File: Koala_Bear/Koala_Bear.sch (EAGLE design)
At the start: 15 parts

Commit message: Added Koala
Change-Id: I1ccdab2cf6fbd4164808b8b310fecc799373998b
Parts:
- removed JP1: (no value), pie:M03MTA1X3
- removed U$2: XT60CONNECTOR, pie:XT60CONNECTOR
- removed U$8: M05, pie:M05
- added MSTRO_PINS: (no value), pie_new:M041X04-MTA
- added MSTRO_PWR: M05, pie:M05
- added SERVO_PWR_12, SERVO_PWR_6: (no value), pie:M02PTH
- added XT60: XT60CONNECTOR, pie_new:XT60CONNECTOR
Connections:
- net N$1 renamed EN
- net N$3 renamed DIODE
- removed net N$5: JP1.3, U$8.1
- new net N$3: MSTRO_PINS.3, MSTRO_PWR.2
- net GND: now also MSTRO_PINS.1, MSTRO_PWR.5, SERVO_PWR_12.1, SERVO_PWR_6.2, XT60.GND; no longer U$2.GND, U$8.5
- net N$2: now also MSTRO_PINS.2, MSTRO_PWR.3; no longer JP1.1, U$8.3
- net N$4: now also MSTRO_PINS.4, MSTRO_PWR.1; no longer JP1.2, U$8.2
- net VIN: now also XT60.12V; no longer U$2.12V
- net VOUT: now also MSTRO_PWR.4, SERVO_PWR_12.2, SERVO_PWR_6.1; no longer U$8.4
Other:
- note added: "BATTERY"
- moved on the sheet: CFF, CIN, COUT1, COUT2, CSS, D1, REN1, REN2, REN3, RFBB, RFBT

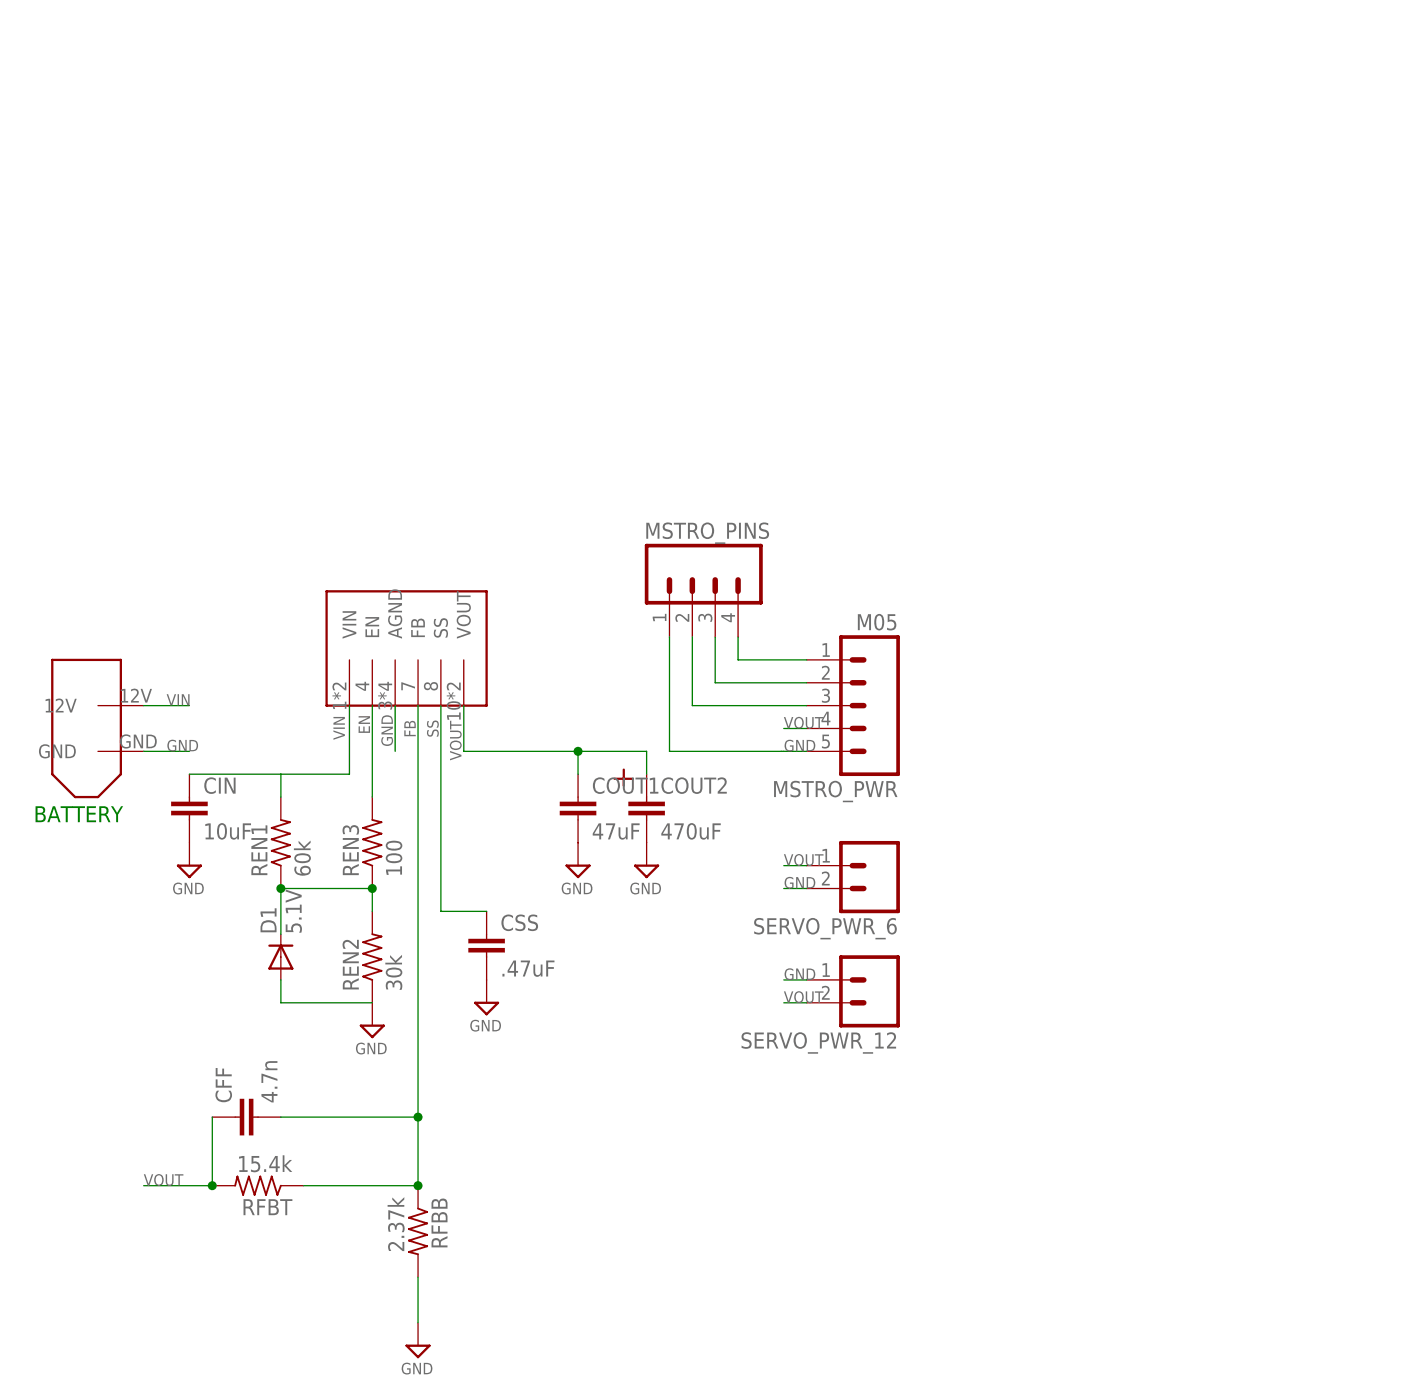
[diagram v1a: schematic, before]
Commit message: Added preliminary LED system. Incomplete.
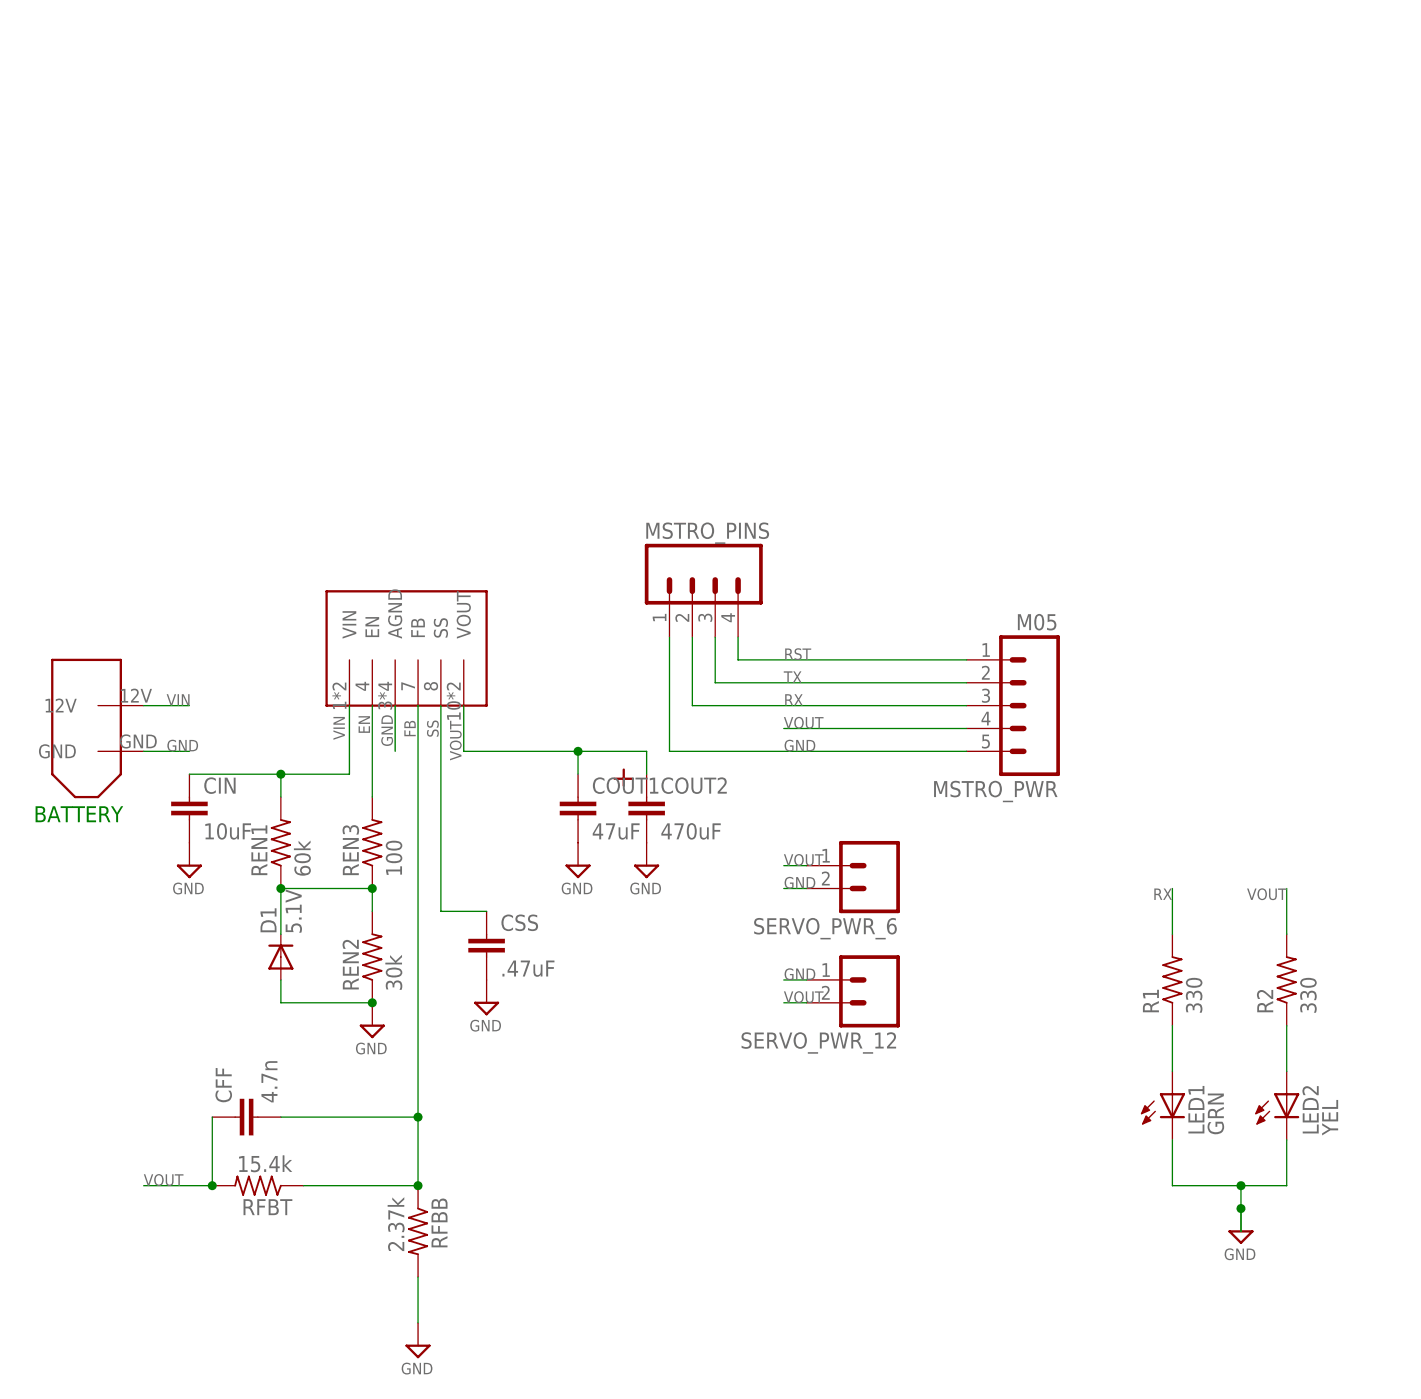
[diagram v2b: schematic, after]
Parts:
- added LED1: GRN, led:LEDCHIP-LED0805
- added LED2: YEL, led:LEDCHIP-LED0805
- added R1, R2: 330, rcl:R-US_R0603
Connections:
- net N$3 renamed TX
- net N$4 renamed RST
- removed net N$2: MSTRO_PINS.2, MSTRO_PWR.3
- new net N$1: LED1.A, R1.1
- new net N$5: LED2.A, R2.1
- new net RX: MSTRO_PINS.2, MSTRO_PWR.3, R1.2
- net GND: now also LED1.C, LED2.C
- net VOUT: now also R2.2
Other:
- moved on the sheet: MSTRO_PWR
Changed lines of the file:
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@@
 <?xml version="1.0" encoding="utf-8"?>
 <!DOCTYPE eagle SYSTEM "eagle.dtd">
-<eagle version="6.2">
+<eagle version="6.5.0">
 <drawing>
 <settings>
@@
 <part name="SERVO_PWR_12" library="pie" deviceset="M02" device="PTH"/>
 <part name="FRAME1" library="pie" deviceset="FRAME-LETTER" device=""/>
+<part name="R1" library="rcl" deviceset="R-US_" device="R0603" value="330"/>
+<part name="R2" library="rcl" deviceset="R-US_" device="R0603" value="330"/>
+<part name="LED1" library="led" deviceset="LED" device="CHIP-LED0805" value="GRN"/>
+<part name="LED2" library="led" deviceset="LED" device="CHIP-LED0805" value="YEL"/>
+<part name="SUPPLY4" library="supply2" deviceset="GND" device=""/>
 </parts>
 <sheets>
@@
 </instance>
 <instance part="XT60" gate="G$1" x="-25.4" y="50.8" smashed="yes" rot="R270"/>
-<instance part="MSTRO_PWR" gate="G$1" x="63.5" y="43.18" smashed="yes" rot="R180">
-<attribute name="VALUE" x="68.58" y="55.88" size="1.778" layer="96" font="vector" rot="R180"/>
-<attribute name="NAME" x="68.58" y="37.338" size="1.778" layer="95" font="vector" rot="R180"/>
+<instance part="MSTRO_PWR" gate="G$1" x="81.28" y="43.18" smashed="yes" rot="R180">
+<attribute name="VALUE" x="86.36" y="55.88" size="1.778" layer="96" font="vector" rot="R180"/>
+<attribute name="NAME" x="86.36" y="37.338" size="1.778" layer="95" font="vector" rot="R180"/>
 </instance>
 <instance part="SERVO_PWR_6" gate="G$1" x="66.04" y="27.94" smashed="yes" rot="R180">
@@
 <attribute name="DRAWING_NAME" x="73.914" y="-66.04" size="2.7432" layer="94" font="vector"/>
 </instance>
+<instance part="R1" gate="G$1" x="99.06" y="15.24" smashed="yes" rot="R90">
+<attribute name="NAME" x="97.5614" y="11.43" size="1.778" layer="95" rot="R90"/>
+<attribute name="VALUE" x="102.362" y="11.43" size="1.778" layer="96" rot="R90"/>
+</instance>
+<instance part="R2" gate="G$1" x="111.76" y="15.24" smashed="yes" rot="R90">
+<attribute name="NAME" x="110.2614" y="11.43" size="1.778" layer="95" rot="R90"/>
+<attribute name="VALUE" x="115.062" y="11.43" size="1.778" layer="96" rot="R90"/>
+</instance>
+<instance part="LED1" gate="G$1" x="99.06" y="2.54" smashed="yes">
+<attribute name="NAME" x="102.616" y="-2.032" size="1.778" layer="95" rot="R90"/>
+<attribute name="VALUE" x="104.775" y="-2.032" size="1.778" layer="96" rot="R90"/>
+</instance>
+<instance part="LED2" gate="G$1" x="111.76" y="2.54" smashed="yes">
+<attribute name="NAME" x="115.316" y="-2.032" size="1.778" layer="95" rot="R90"/>
+<attribute name="VALUE" x="117.475" y="-2.032" size="1.778" layer="96" rot="R90"/>
+</instance>
+<instance part="SUPPLY4" gate="GND" x="106.68" y="-12.7" smashed="yes">
+<attribute name="VALUE" x="104.775" y="-15.875" size="1.27" layer="96"/>
+</instance>
 </instances>
 <busses>
@@
 <wire x1="0" y1="15.24" x2="0" y2="12.7" width="0.1524" layer="91"/>
 <wire x1="0" y1="12.7" x2="10.16" y2="12.7" width="0.1524" layer="91"/>
+<junction x="10.16" y="12.7"/>
 </segment>
 <segment>
@@
 <segment>
 <pinref part="MSTRO_PWR" gate="G$1" pin="5"/>
-<wire x1="55.626" y1="40.64" x2="55.88" y2="40.64" width="0.1524" layer="91"/>
 <label x="55.88" y="40.64" size="1.27" layer="95" font="vector"/>
 <pinref part="MSTRO_PINS" gate="G$1" pin="1"/>
-<wire x1="55.88" y1="40.64" x2="58.42" y2="40.64" width="0.1524" layer="91"/>
 <wire x1="43.18" y1="53.34" x2="43.18" y2="40.64" width="0.1524" layer="91"/>
-<wire x1="43.18" y1="40.64" x2="55.626" y2="40.64" width="0.1524" layer="91"/>
+<wire x1="43.18" y1="40.64" x2="76.2" y2="40.64" width="0.1524" layer="91"/>
 </segment>
 <segment>
@@
 <wire x1="-15.24" y1="40.64" x2="-10.16" y2="40.64" width="0.1524" layer="91"/>
 <label x="-12.7" y="40.64" size="1.27" layer="95" font="vector"/>
+</segment>
+<segment>
+<pinref part="LED1" gate="G$1" pin="C"/>
+<wire x1="99.06" y1="-2.54" x2="99.06" y2="-7.62" width="0.1524" layer="91"/>
+<pinref part="LED2" gate="G$1" pin="C"/>
+<wire x1="99.06" y1="-7.62" x2="106.68" y2="-7.62" width="0.1524" layer="91"/>
+<wire x1="106.68" y1="-7.62" x2="111.76" y2="-7.62" width="0.1524" layer="91"/>
+<wire x1="111.76" y1="-7.62" x2="111.76" y2="-2.54" width="0.1524" layer="91"/>
+<junction x="106.68" y="-7.62"/>
+<wire x1="106.68" y1="-7.62" x2="106.68" y2="-10.16" width="0.1524" layer="91"/>
+<pinref part="SUPPLY4" gate="GND" pin="GND"/>
+<wire x1="106.68" y1="-10.16" x2="106.68" y2="-12.7" width="0.1524" layer="91"/>
+<junction x="106.68" y="-10.16"/>
 </segment>
 </net>
@@
 <pinref part="REN1" gate="G$1" pin="2"/>
 <wire x1="0" y1="35.56" x2="0" y2="38.1" width="0.1524" layer="91"/>
+<junction x="0" y="38.1"/>
 </segment>
 <segment>
@@
 <label x="20.066" y="39.624" size="1.27" layer="95" font="vector" rot="R90"/>
 <wire x1="20.32" y1="40.64" x2="33.02" y2="40.64" width="0.1524" layer="91"/>
-<wire x1="33.02" y1="40.64" x2="40.64" y2="40.64" width="0.1524" layer="91"/>
+<wire x1="40.64" y1="38.1" x2="40.64" y2="40.64" width="0.1524" layer="91"/>
+<wire x1="40.64" y1="40.64" x2="33.02" y2="40.64" width="0.1524" layer="91"/>
 <pinref part="COUT2" gate="G$1" pin="POS"/>
-<wire x1="40.64" y1="38.1" x2="40.64" y2="40.64" width="0.1524" layer="91"/>
 <junction x="33.02" y="40.64"/>
 </segment>
@@
 <segment>
 <pinref part="MSTRO_PWR" gate="G$1" pin="4"/>
-<wire x1="58.42" y1="43.18" x2="55.88" y2="43.18" width="0.1524" layer="91"/>
+<wire x1="76.2" y1="43.18" x2="55.88" y2="43.18" width="0.1524" layer="91"/>
 <label x="55.88" y="43.18" size="1.27" layer="95" font="vector"/>
 </segment>
@@
 <wire x1="58.42" y1="12.7" x2="55.88" y2="12.7" width="0.1524" layer="91"/>
 <label x="55.88" y="12.7" size="1.27" layer="95" font="vector"/>
+</segment>
+<segment>
+<pinref part="R2" gate="G$1" pin="2"/>
+<wire x1="111.76" y1="20.32" x2="111.76" y2="25.4" width="0.1524" layer="91"/>
+<label x="111.76" y="25.4" size="1.27" layer="95" rot="R180"/>
 </segment>
 </net>
@@
 </segment>
 </net>
-<net name="N$2" class="0">
+<net name="RX" class="0">
 <segment>
 <pinref part="MSTRO_PINS" gate="G$1" pin="2"/>
 <wire x1="45.72" y1="53.34" x2="45.72" y2="45.72" width="0.1524" layer="91"/>
 <pinref part="MSTRO_PWR" gate="G$1" pin="3"/>
-<wire x1="45.72" y1="45.72" x2="58.42" y2="45.72" width="0.1524" layer="91"/>
-</segment>
-</net>
-<net name="N$3" class="0">
+<wire x1="45.72" y1="45.72" x2="76.2" y2="45.72" width="0.1524" layer="91"/>
+<label x="55.88" y="45.72" size="1.27" layer="95"/>
+</segment>
+<segment>
+<pinref part="R1" gate="G$1" pin="2"/>
+<wire x1="99.06" y1="20.32" x2="99.06" y2="25.4" width="0.1524" layer="91"/>
+<label x="99.06" y="25.4" size="1.27" layer="95" rot="R180"/>
+</segment>
+</net>
+<net name="TX" class="0">
 <segment>
 <pinref part="MSTRO_PINS" gate="G$1" pin="3"/>
 <wire x1="48.26" y1="53.34" x2="48.26" y2="48.26" width="0.1524" layer="91"/>
 <pinref part="MSTRO_PWR" gate="G$1" pin="2"/>
-<wire x1="48.26" y1="48.26" x2="58.42" y2="48.26" width="0.1524" layer="91"/>
-</segment>
-</net>
-<net name="N$4" class="0">
+<wire x1="48.26" y1="48.26" x2="76.2" y2="48.26" width="0.1524" layer="91"/>
+<label x="55.88" y="48.26" size="1.27" layer="95"/>
+</segment>
+</net>
+<net name="RST" class="0">
 <segment>
 <pinref part="MSTRO_PINS" gate="G$1" pin="4"/>
 <wire x1="50.8" y1="53.34" x2="50.8" y2="50.8" width="0.1524" layer="91"/>
 <pinref part="MSTRO_PWR" gate="G$1" pin="1"/>
-<wire x1="50.8" y1="50.8" x2="58.42" y2="50.8" width="0.1524" layer="91"/>
-</segment>
-</net>
+<wire x1="50.8" y1="50.8" x2="76.2" y2="50.8" width="0.1524" layer="91"/>
+<label x="55.88" y="50.8" size="1.27" layer="95"/>
+</segment>
+</net>
+<net name="N$1" class="0">
+<segment>
+<pinref part="R1" gate="G$1" pin="1"/>
+<wire x1="99.06" y1="10.16" x2="99.06" y2="5.08" width="0.1524" layer="91"/>
+<pinref part="LED1" gate="G$1" pin="A"/>
+</segment>
+</net>
+<net name="N$5" class="0">
+<segment>
+<pinref part="R2" gate="G$1" pin="1"/>
+<wire x1="111.76" y1="10.16" x2="111.76" y2="5.08" width="0.1524" layer="91"/>
+<pinref part="LED2" gate="G$1" pin="A"/>
+</segment>
+</net>

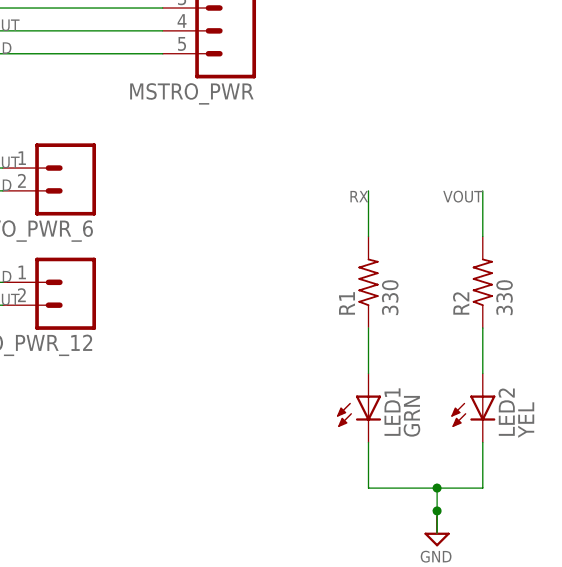
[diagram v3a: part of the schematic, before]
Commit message: Fixed critical items as per  review of 10/11.
Fixed GND orientation of one LED
Moved one LED farther away from large adjacent chips
Caught and fixed all unrouted traces
Fixed T-junction angle
Silkscreen updated to include current info.
--Still needs fixing by Rev B--
1. Moving LEDs closer together
2. Using identical orientation for all passives
3. Deleting superfluous holes and creating 1 new one as per Yip's
request

As per Doug at the 10/12 worksession, the above will work and is good
enough for a first draft, but more can be done (by Rev A if time
permits)
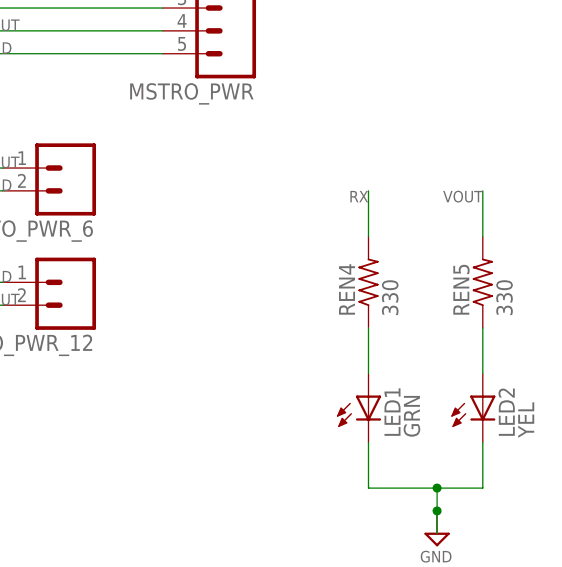
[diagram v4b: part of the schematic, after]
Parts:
- renumbered R1 to REN4, R2 to REN5
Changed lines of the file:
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@@
 <attribute name="REVISION" value="A"/>
 </part>
-<part name="R1" library="rcl" deviceset="R-US_" device="R0603" value="330"/>
-<part name="R2" library="rcl" deviceset="R-US_" device="R0603" value="330"/>
+<part name="REN4" library="rcl" deviceset="R-US_" device="R0603" value="330"/>
+<part name="REN5" library="rcl" deviceset="R-US_" device="R0603" value="330"/>
 <part name="LED1" library="led" deviceset="LED" device="CHIP-LED0805" value="GRN"/>
 <part name="LED2" library="led" deviceset="LED" device="CHIP-LED0805" value="YEL"/>
@@
 <attribute name="REVISION" x="147.32" y="-76.835" size="2.7432" layer="94" font="vector"/>
 </instance>
-<instance part="R1" gate="G$1" x="99.06" y="15.24" smashed="yes" rot="R90">
+<instance part="REN4" gate="G$1" x="99.06" y="15.24" smashed="yes" rot="R90">
 <attribute name="NAME" x="97.5614" y="11.43" size="1.778" layer="95" rot="R90"/>
 <attribute name="VALUE" x="102.362" y="11.43" size="1.778" layer="96" rot="R90"/>
 </instance>
-<instance part="R2" gate="G$1" x="111.76" y="15.24" smashed="yes" rot="R90">
+<instance part="REN5" gate="G$1" x="111.76" y="15.24" smashed="yes" rot="R90">
 <attribute name="NAME" x="110.2614" y="11.43" size="1.778" layer="95" rot="R90"/>
 <attribute name="VALUE" x="115.062" y="11.43" size="1.778" layer="96" rot="R90"/>
@@
 </segment>
 <segment>
-<pinref part="R2" gate="G$1" pin="2"/>
+<pinref part="REN5" gate="G$1" pin="2"/>
 <wire x1="111.76" y1="20.32" x2="111.76" y2="25.4" width="0.1524" layer="91"/>
 <label x="111.76" y="25.4" size="1.27" layer="95" rot="R180"/>
@@
 </segment>
 <segment>
-<pinref part="R1" gate="G$1" pin="2"/>
+<pinref part="REN4" gate="G$1" pin="2"/>
 <wire x1="99.06" y1="20.32" x2="99.06" y2="25.4" width="0.1524" layer="91"/>
 <label x="99.06" y="25.4" size="1.27" layer="95" rot="R180"/>
@@
 <net name="N$1" class="0">
 <segment>
-<pinref part="R1" gate="G$1" pin="1"/>
+<pinref part="REN4" gate="G$1" pin="1"/>
 <wire x1="99.06" y1="10.16" x2="99.06" y2="5.08" width="0.1524" layer="91"/>
 <pinref part="LED1" gate="G$1" pin="A"/>
@@
 <net name="N$5" class="0">
 <segment>
-<pinref part="R2" gate="G$1" pin="1"/>
+<pinref part="REN5" gate="G$1" pin="1"/>
 <wire x1="111.76" y1="10.16" x2="111.76" y2="5.08" width="0.1524" layer="91"/>
 <pinref part="LED2" gate="G$1" pin="A"/>
